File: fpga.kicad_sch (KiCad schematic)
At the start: 2 parts, among them U1 ICE40HX4K-TQ144

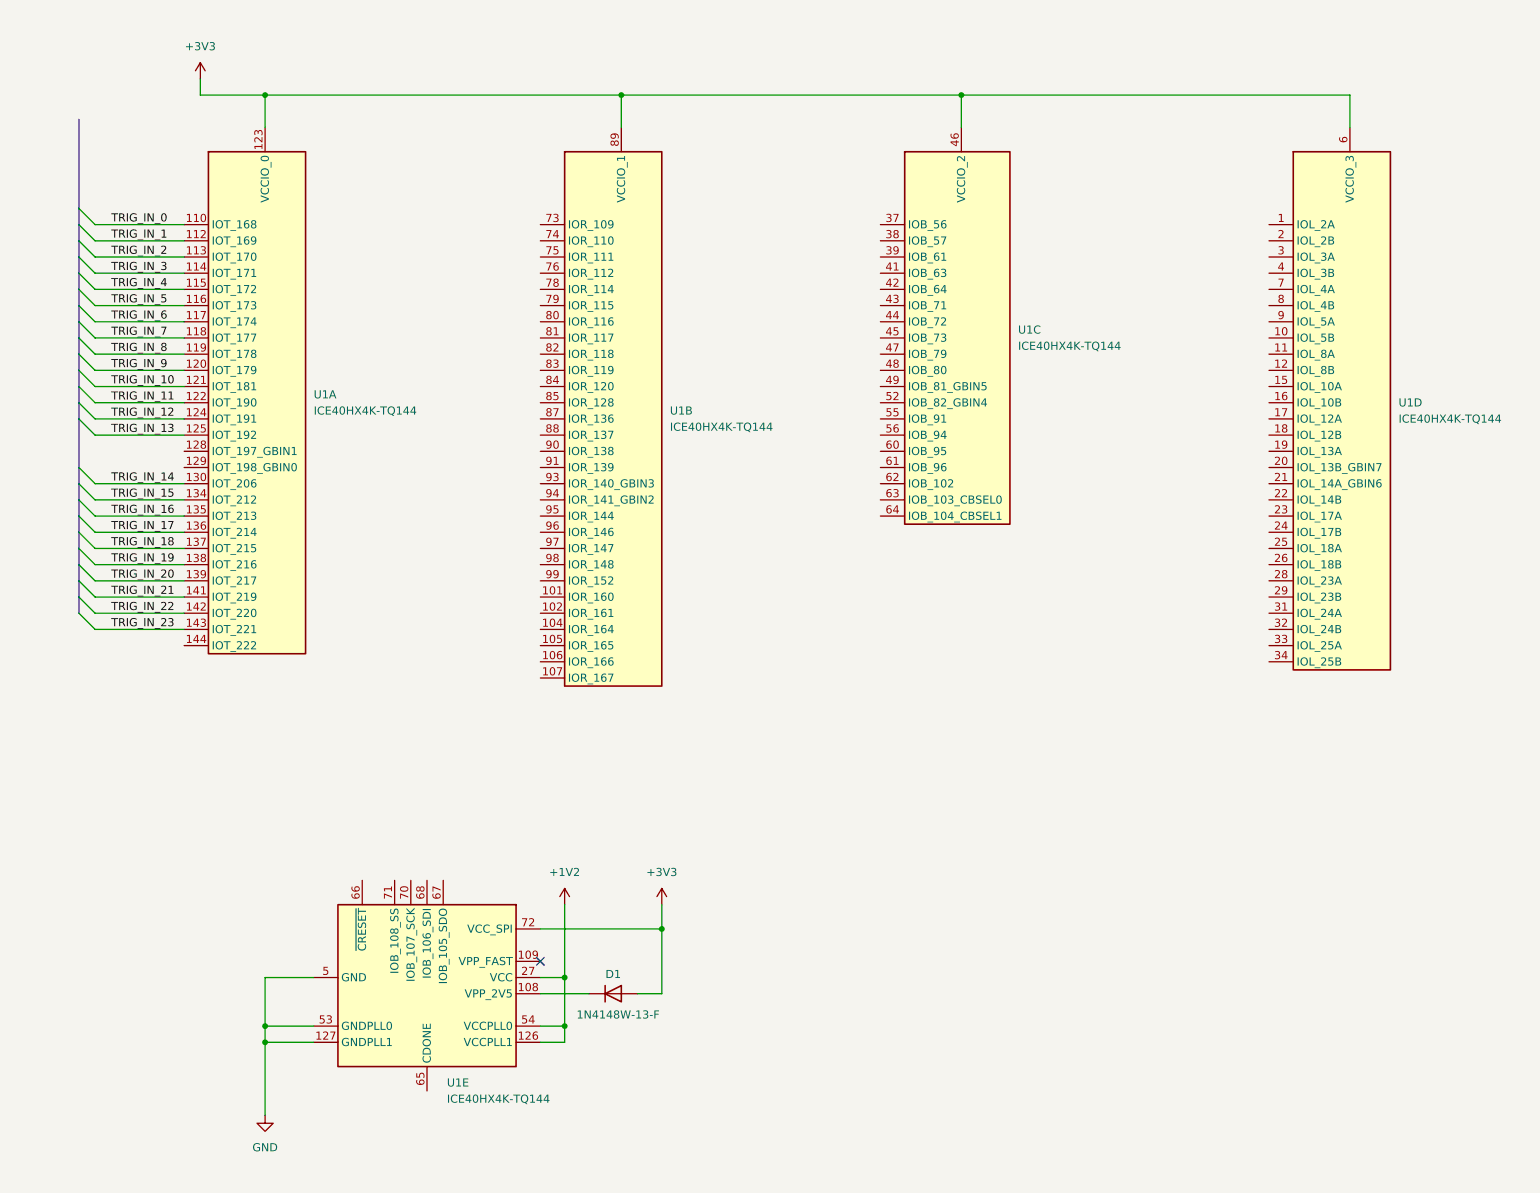
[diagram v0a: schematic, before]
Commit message: Added SD card readers and USB-C for power in.
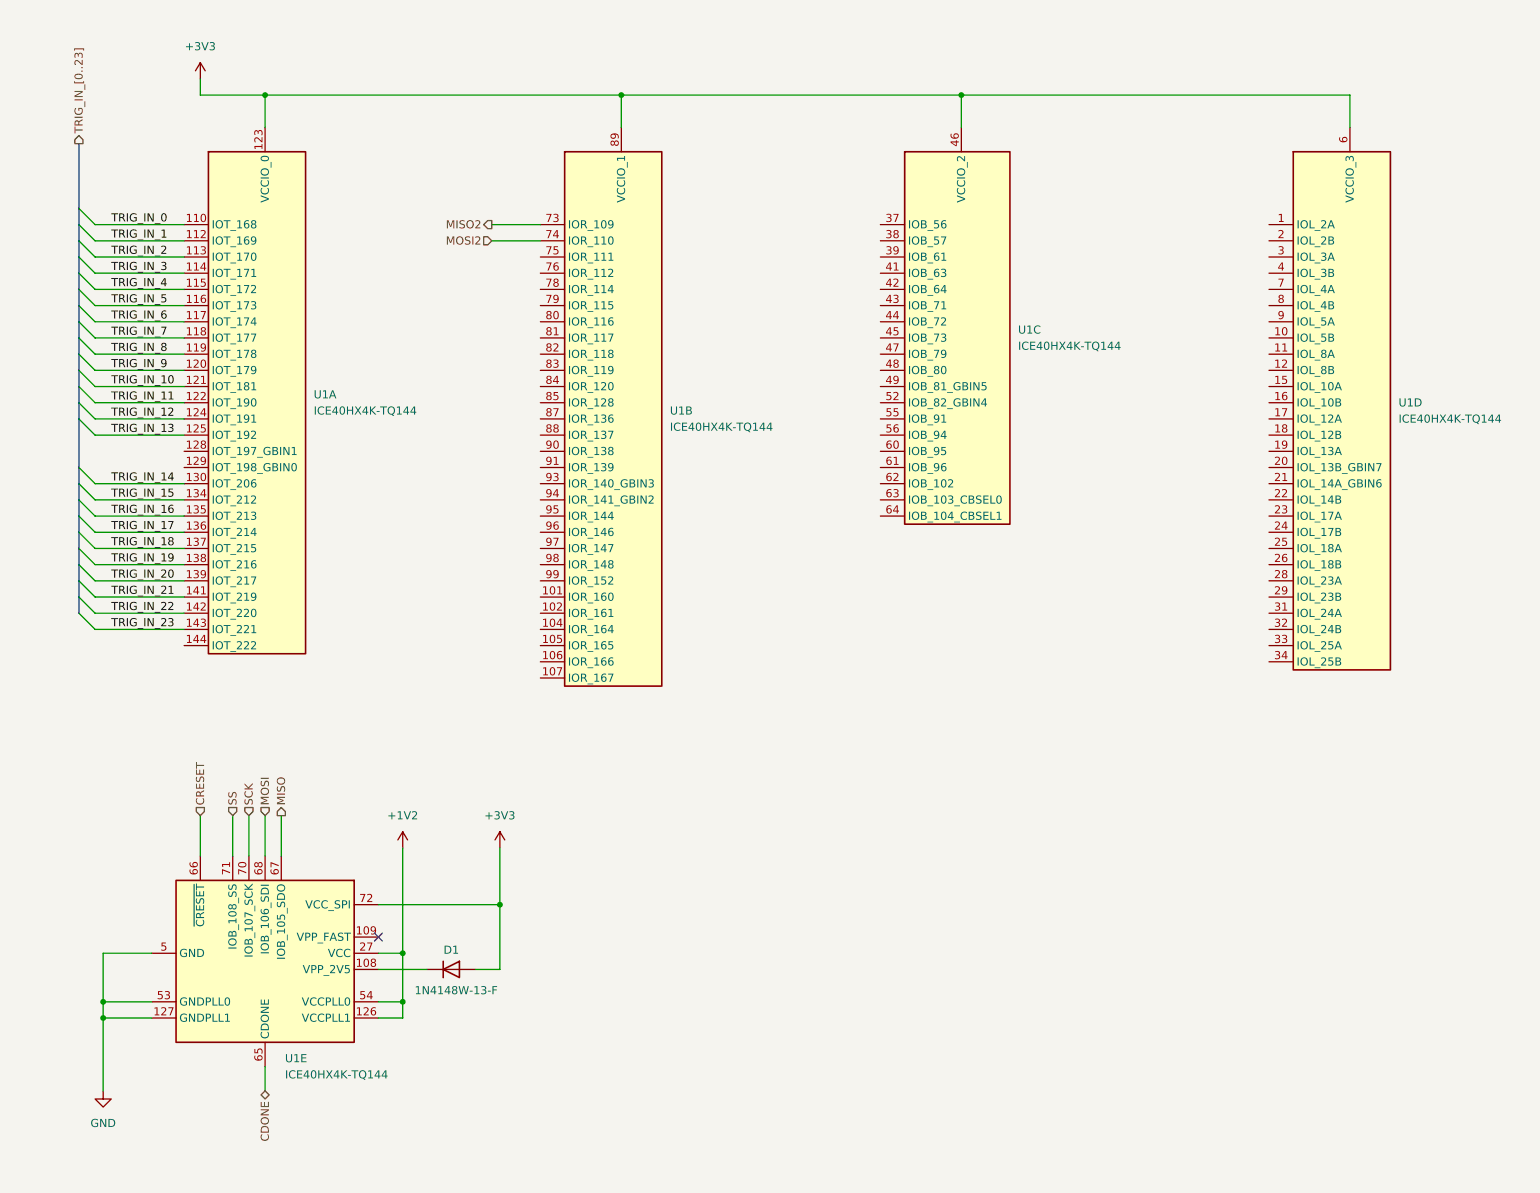
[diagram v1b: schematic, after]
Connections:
- net MISO2: now reaches U1.73 (IOR_109)
- net MOSI2: now reaches U1.74 (IOR_110)
- net CDONE: now reaches U1.65 (CDONE)
- net CRESET: now reaches U1.66 (~{CRESET})
- net MISO: now reaches U1.67 (IOB_105_SDO)
- net MOSI: now reaches U1.68 (IOB_106_SDI)
- net SCK: now reaches U1.70 (IOB_107_SCK)
- net SS: now reaches U1.71 (IOB_108_SS)
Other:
- moved on the sheet: D1, U1E

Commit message: cleanup
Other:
- moved on the sheet: U1A

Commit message: rewire
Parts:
- added D12, D3: LED, symbol Device:LED
- added Q3, Q4: AO3400A, symbol Transistor_FET:Q_NMOS_GSD
- added R90, R94: 100R, symbol Device:R
- added R91, R95: 10k, symbol Device:R
- added R92, R93: 220R, symbol Device:R
- D1: value 1N4148W-13-F -> 1N4148W
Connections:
- net +3V3: now also R92.2, R93.2
- net GND: now also Q3.2 (S), Q4.2 (S), R91.2, R95.2
- net MISO renamed SO
- net MOSI renamed SI
- new net: D12.1 (K), Q4.3 (D)
- new net: D12.2 (A), R93.1
- new net: D3.2 (A), R92.1
- new net: Q4.1 (G), R94.2, R95.1
- new net: Q3.1 (G), R90.2, R91.1
- new net: D3.1 (K), Q3.3 (D)
- new net PLL_LOCK: R90.1
- new net TRIGGERED: R94.1
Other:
- moved on the sheet: D1, U1E
